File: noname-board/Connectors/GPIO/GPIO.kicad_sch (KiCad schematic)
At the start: 0 parts

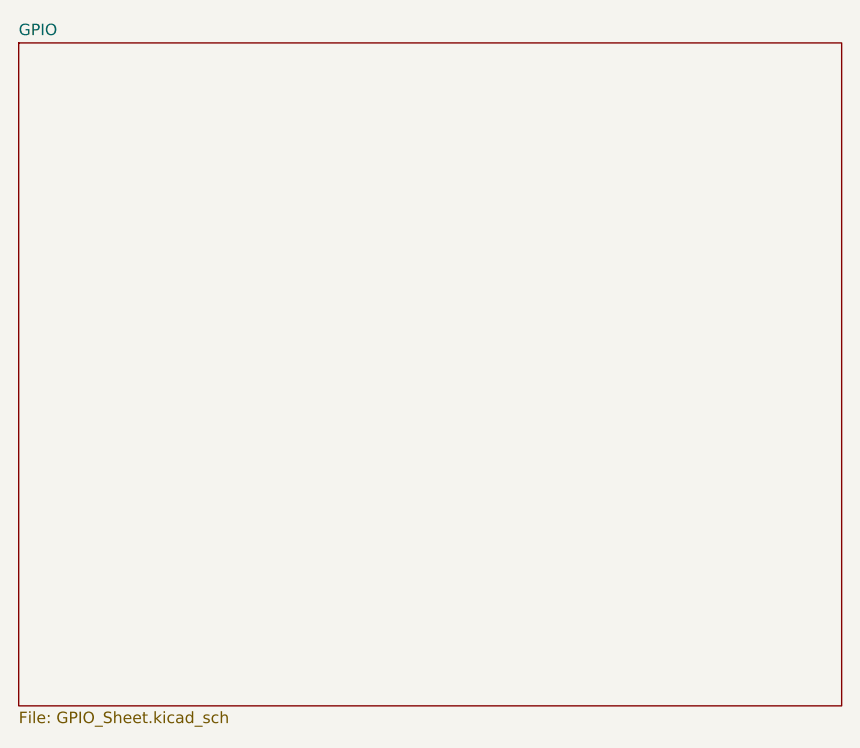
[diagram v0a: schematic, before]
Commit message: GPIO, USBC
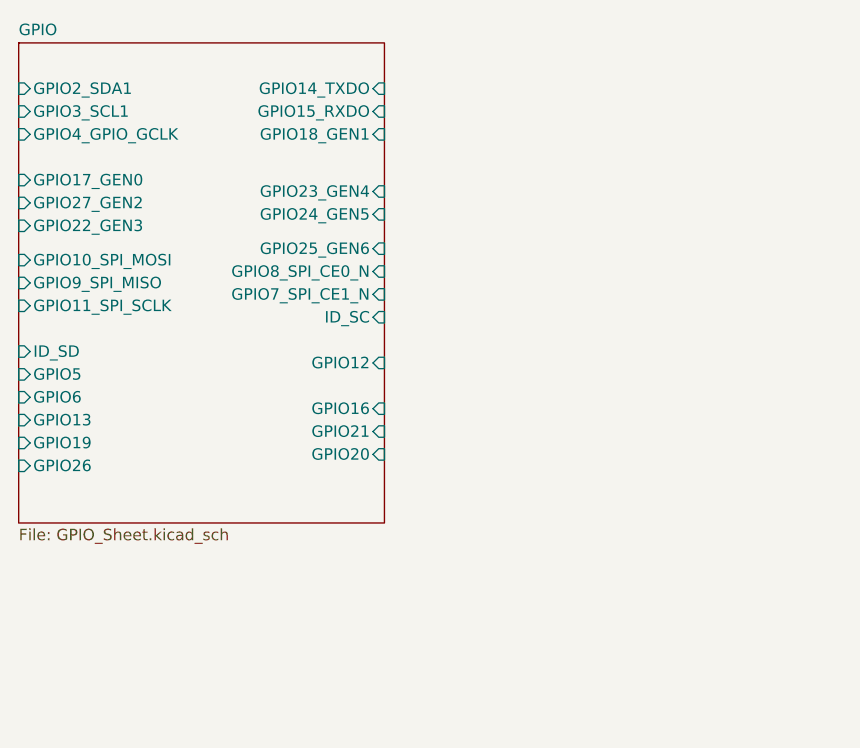
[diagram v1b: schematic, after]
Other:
- sheet GPIO ports: added GPIO10_SPI_MOSI, GPIO11_SPI_SCLK, GPIO12, GPIO13, GPIO14_TXDO, GPIO15_RXDO, GPIO16, GPIO17_GEN0, GPIO18_GEN1, GPIO19, GPIO20, GPIO21, GPIO22_GEN3, GPIO23_GEN4, GPIO24_GEN5, GPIO25_GEN6, GPIO26, GPIO27_GEN2, GPIO2_SDA1, GPIO3_SCL1, GPIO4_GPIO_GCLK, GPIO5, GPIO6, GPIO7_SPI_CE1_N, GPIO8_SPI_CE0_N, GPIO9_SPI_MISO, ID_SC, ID_SD; removed none
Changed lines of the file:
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@@
 (kicad_sch (version 20230121) (generator eeschema)
   (paper "A4")
-  (sheet (at 137.16 54.61) (size 91.44 73.66) (fields_autoplaced)
+  (sheet (at 137.16 54.61) (size 40.64 53.34) (fields_autoplaced)
     (stroke (width 0.1524) (type solid))
     (fill (color 0 0 0 0.0000))
@@
       (effects (font (size 1.27 1.27)) (justify left bottom))
     )
-    (property "Sheetfile" "GPIO_Sheet.kicad_sch" (at 137.16 128.8546 0)
+    (property "Sheetfile" "GPIO_Sheet.kicad_sch" (at 137.16 108.5346 0)
       (effects (font (size 1.27 1.27)) (justify left top))
     )
+    (pin "GPIO14_TXDO" input (at 177.8 59.69 0)
+      (effects (font (size 1.27 1.27)) (justify right))
+    )
+    (pin "GPIO18_GEN1" input (at 177.8 64.77 0)
+      (effects (font (size 1.27 1.27)) (justify right))
+    )
+    (pin "GPIO15_RXDO" input (at 177.8 62.23 0)
+      (effects (font (size 1.27 1.27)) (justify right))
+    )
+    (pin "GPIO23_GEN4" input (at 177.8 71.12 0)
+      (effects (font (size 1.27 1.27)) (justify right))
+    )
+    (pin "GPIO24_GEN5" input (at 177.8 73.66 0)
+      (effects (font (size 1.27 1.27)) (justify right))
+    )
+    (pin "GPIO8_SPI_CE0_N" input (at 177.8 80.01 0)
+      (effects (font (size 1.27 1.27)) (justify right))
+    )
+    (pin "GPIO25_GEN6" input (at 177.8 77.47 0)
+      (effects (font (size 1.27 1.27)) (justify right))
+    )
+    (pin "GPIO7_SPI_CE1_N" input (at 177.8 82.55 0)
+      (effects (font (size 1.27 1.27)) (justify right))
+    )
+    (pin "ID_SC" input (at 177.8 85.09 0)
+      (effects (font (size 1.27 1.27)) (justify right))
+    )
+    (pin "GPIO12" input (at 177.8 90.17 0)
+      (effects (font (size 1.27 1.27)) (justify right))
+    )
+    (pin "GPIO16" input (at 177.8 95.25 0)
+      (effects (font (size 1.27 1.27)) (justify right))
+    )
+    (pin "GPIO21" input (at 177.8 97.79 0)
+      (effects (font (size 1.27 1.27)) (justify right))
+    )
+    (pin "GPIO20" input (at 177.8 100.33 0)
+      (effects (font (size 1.27 1.27)) (justify right))
+    )
+    (pin "GPIO19" input (at 137.16 99.06 180)
+      (effects (font (size 1.27 1.27)) (justify left))
+    )
+    (pin "GPIO26" input (at 137.16 101.6 180)
+      (effects (font (size 1.27 1.27)) (justify left))
+    )
+    (pin "ID_SD" input (at 137.16 88.9 180)
+      (effects (font (size 1.27 1.27)) (justify left))
+    )
+    (pin "GPIO6" input (at 137.16 93.98 180)
+      (effects (font (size 1.27 1.27)) (justify left))
+    )
+    (pin "GPIO13" input (at 137.16 96.52 180)
+      (effects (font (size 1.27 1.27)) (justify left))
+    )
+    (pin "GPIO5" input (at 137.16 91.44 180)
+      (effects (font (size 1.27 1.27)) (justify left))
+    )
+    (pin "GPIO4_GPIO_GCLK" input (at 137.16 64.77 180)
+      (effects (font (size 1.27 1.27)) (justify left))
+    )
+    (pin "GPIO2_SDA1" input (at 137.16 59.69 180)
+      (effects (font (size 1.27 1.27)) (justify left))
+    )
+    (pin "GPIO3_SCL1" input (at 137.16 62.23 180)
+      (effects (font (size 1.27 1.27)) (justify left))
+    )
+    (pin "GPIO17_GEN0" input (at 137.16 69.85 180)
+      (effects (font (size 1.27 1.27)) (justify left))
+    )
+    (pin "GPIO22_GEN3" input (at 137.16 74.93 180)
+      (effects (font (size 1.27 1.27)) (justify left))
+    )
+    (pin "GPIO27_GEN2" input (at 137.16 72.39 180)
+      (effects (font (size 1.27 1.27)) (justify left))
+    )
+    (pin "GPIO11_SPI_SCLK" input (at 137.16 83.82 180)
+      (effects (font (size 1.27 1.27)) (justify left))
+    )
+    (pin "GPIO10_SPI_MOSI" input (at 137.16 78.74 180)
+      (effects (font (size 1.27 1.27)) (justify left))
+    )
+    (pin "GPIO9_SPI_MISO" input (at 137.16 81.28 180)
+      (effects (font (size 1.27 1.27)) (justify left))
+    )
     (instances

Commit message: We went thru eveeeryyything
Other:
- sheet GPIO ports: added 3V3, 5V, GND; removed none
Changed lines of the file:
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@@
+      (effects (font (size 1.27 1.27)) (justify left))
+    )
+    (pin "5V" input (at 137.16 57.15 180)
+      (effects (font (size 1.27 1.27)) (justify left))
+    )
+    (pin "3V3" input (at 177.8 57.15 0)
+      (effects (font (size 1.27 1.27)) (justify right))
+    )
+    (pin "GND" input (at 172.72 107.95 270)
       (effects (font (size 1.27 1.27)) (justify left))
     )
